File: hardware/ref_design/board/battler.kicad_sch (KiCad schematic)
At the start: 9 parts

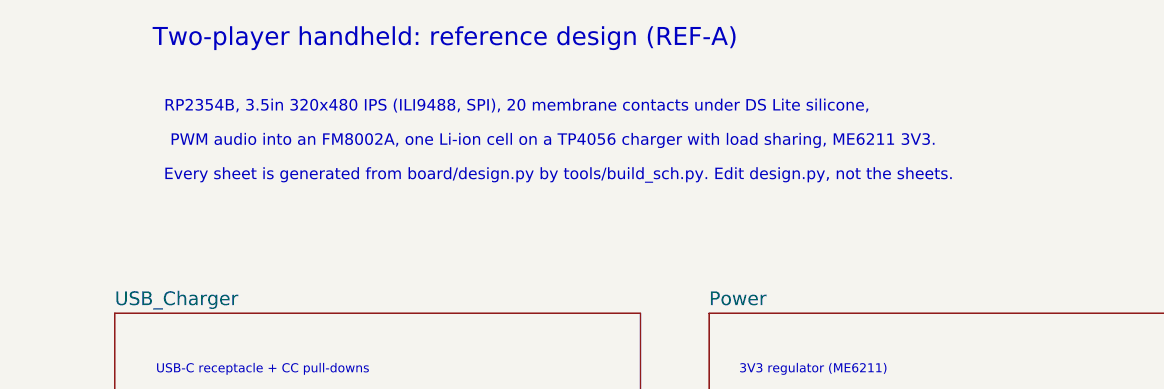
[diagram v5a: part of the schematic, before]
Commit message: ref_design: ER-TFT024IPS-3 panel pin map, R61 2.4k
The 2.4in ST7789V panel on the same 50-pin FPC: K3/K4 on pins 4-5 join
K1/K2's sinks (two LEDs a sink), IM3-0 on pins 6-9 strapped 1110 (4-line
serial II, SDI in and SDO out, as before), D/CX on 36 and SCL on 37.
R61 3.9k -> 2.4k: 0.077 V on 2.2 ohm, 35 mA a sink, 70 mA in all (the
panel's typical, 80 max). Pin review, schematic notes and docs follow.

Co-Authored-By: Claude Opus 5.5 <noreply@anthropic.com>
Claude-Session: https://claude.ai/code/session_01Y3mFMxLYqNeyyedvbYuRwX
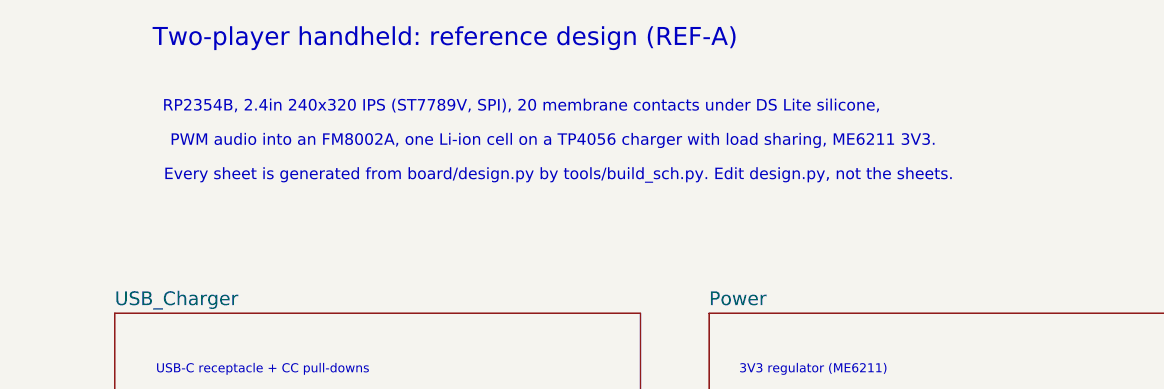
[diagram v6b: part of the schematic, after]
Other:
- note added: "RP2354B, 2.4in 240x320 IPS (ST7789V, SPI), 20 membrane contacts under DS Lite silicone,"
- note removed: "RP2354B, 3.5in 320x480 IPS (ILI9488, SPI), 20 membrane contacts under DS Lite silicone,"
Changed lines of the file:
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@@
 		)
 	)
-	(text "RP2354B, 3.5in 320x480 IPS (ILI9488, SPI), 20 membrane contacts under DS Lite silicone,"
+	(text "RP2354B, 2.4in 240x320 IPS (ST7789V, SPI), 20 membrane contacts under DS Lite silicone,"
 		(exclude_from_sim no)
-		(at 65.0081 27.94 0)
+		(at 65.5218 27.94 0)
 		(effects
 			(font

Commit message: WIP: row 19 layout, one-sided: no speaker, core in the left bezel (unrouted)
Since the one-sided-assembly ruling the work has been row 19, not row 18:
the speaker, J4 and the FM8002A circuit are out of design.py (GPIO8 and
GPIO11 unconnected), the cell sits in its hole, every SMT part is on the
front, and the RP2354B core moved from the back to the left bezel. Row 18
was ruled out on geometry first: with the core on the front it needs most of
one side bezel, and the speaker hole, J4 and three SOIC-8s had nowhere left.

Earlier row-19 placements (core in the right bezel) left 18-30 connections
open after Freerouting: J1's pads faced the cell hole with 1.3 mm to spare,
and seat 2's lines had to cross the whole board past the charger. This
commit has the core and the charger swapped, the hole's lead pocket cut to
1 mm and the original pin map; not routed yet.

Co-Authored-By: Claude Opus 5.5 <noreply@anthropic.com>
Claude-Session: https://claude.ai/code/session_01Y3mFMxLYqNeyyedvbYuRwX
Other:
- removed sheet Audio
- note added: "one Li-ion cell (in a hole in the board) on a TP4056 charger with load sharing, ME6211 3V3, no audio."
- note removed: "PWM audio into an FM8002A, one Li-ion cell on a TP4056 charger with load sharing, ME6211 3V3."
- note removed: "PWM low-pass filter, DC block"
- note removed: "amplifier (FM8002A) and supply"
- note removed: "shutdown control"
- note removed: "speaker pads J4"
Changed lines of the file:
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@@
 		)
 	)
-	(text "PWM audio into an FM8002A, one Li-ion cell on a TP4056 charger with load sharing, ME6211 3V3."
-		(exclude_from_sim no)
-		(at 69.0347 31.75 0)
+	(text "one Li-ion cell (in a hole in the board) on a TP4056 charger with load sharing, ME6211 3V3, no audio."
+		(exclude_from_sim no)
+		(at 71.7283 31.75 0)
 		(effects
 			(font
@@
 		)
 	)
-	(text "PWM low-pass filter, DC block"
-		(exclude_from_sim no)
-		(at 166.632 107.95 0)
-		(effects
-			(font
-				(size 1 1)
-			)
-		)
-	)
-	(text "amplifier (FM8002A) and supply"
-		(exclude_from_sim no)
-		(at 167.0835 112.4 0)
-		(effects
-			(font
-				(size 1 1)
-			)
-		)
-	)
-	(text "shutdown control"
-		(exclude_from_sim no)
-		(at 161.346 116.85 0)
-		(effects
-			(font
-				(size 1 1)
-			)
-		)
-	)
-	(text "speaker pads J4"
-		(exclude_from_sim no)
-		(at 161.108 121.3 0)
-		(effects
-			(font
-				(size 1 1)
-			)
-		)
-	)
 	(text "seat 1 and seat 2 contacts"
 		(exclude_from_sim no)
-		(at 231.433 107.95 0)
+		(at 165.393 107.95 0)
 		(effects
 			(font
@@
 	(text "Start/Select per seat (P1 Start"
 		(exclude_from_sim no)
-		(at 232.9315 112.4 0)
+		(at 166.8915 112.4 0)
 		(effects
 			(font
@@
 	(text "is the power button),"
 		(exclude_from_sim no)
-		(at 228.957 116.85 0)
+		(at 162.917 116.85 0)
 		(effects
 			(font
@@
 	(text "20 contacts, one GPIO each"
 		(exclude_from_sim no)
-		(at 231.647 121.3 0)
+		(at 165.607 121.3 0)
 		(effects
 			(font
@@
 			(color 0 0 0 0)
 		)
-		(property "Sheetname" "Audio"
+		(property "Sheetname" "Buttons"
 			(at 152.4 100.8884 0)
 			(show_name no)
@@
 			)
 		)
-		(property "Sheetfile" "audio.kicad_sch"
+		(property "Sheetfile" "buttons.kicad_sch"
 			(at 152.4 135.2184 0)
 			(show_name no)
@@
 				)
 			)
-		)
-	)
-	(sheet
-		(at 218.44 101.6)
-		(size 58.42 33.02)
-		(exclude_from_sim no)
-		(in_bom yes)
-		(on_board yes)
-		(dnp no)
-		(stroke
-			(width 0.1524)
-			(type solid)
-		)
-		(fill
-			(color 0 0 0 0)
-		)
-		(property "Sheetname" "Buttons"
-			(at 218.44 100.8884 0)
-			(show_name no)
-			(do_not_autoplace no)
-			(effects
-				(font
-					(size 1.524 1.524)
-				)
-				(justify left bottom)
-			)
-		)
-		(property "Sheetfile" "buttons.kicad_sch"
-			(at 218.44 135.2184 0)
-			(show_name no)
-			(do_not_autoplace no)
-			(effects
-				(font
-					(size 1.27 1.27)
-				)
-				(justify left top)
-			)
-		)
-		(instances
-			(project "battler"
-				(path "/8922e0a8-6f76-52f6-b0ec-4de6a784796f"
-					(page "9")
-				)
-			)

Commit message: WIP: speaker on the board's top in the right bezel, audio back; 5 nets unrouted
The FM8002A circuit returns as before row 19 (GPIO8 AUDIO_PWM, GPIO11 AMP_EN,
gain 2, J4 PicoBlade for the speaker's plug). The speaker (15 x 10, hand-fitted)
lies face up in the right bezel below the cell's hole: a rule area keeps parts
(not copper) out of it plus 0.5 mm, outline and label on the silkscreen. J1,
the speaker and J4 with its plug don't all fit in that bezel, so J1 went back up
its wall to the case's own y (beside the hole); usb_pair() drops the pair to the
back beside J1's pads. J4 is machine-placed again (out of NO_ASSEMBLY).

Open: 5 connections (CHG_TEMP, CHG_OFF, CC2_SENSE, SR_CLK, a GND pour island),
route.py --finish crashes in Space() (SwigPyObject), Q3 in the cluster's 0.5 mm
retainer band. case/CELLCUT_FOR_CASE.md has the speaker, grille and J4 notes.

Co-Authored-By: Claude Opus 5.5 <noreply@anthropic.com>
Claude-Session: https://claude.ai/code/session_01Y3mFMxLYqNeyyedvbYuRwX
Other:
- added sheet Audio (audio.kicad_sch)
- note added: "PWM low-pass filter, DC block"
- note added: "amplifier (FM8002A) and supply"
- note added: "one Li-ion cell (in a hole in the board) on a BQ24073 charger, ME6211 3V3, PWM audio into an FM8002A."
- note added: "shutdown control"
- note added: "speaker plug J4"
- note removed: "one Li-ion cell (in a hole in the board) on a TP4056 charger with load sharing, ME6211 3V3, no audio."
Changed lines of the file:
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@@
 		)
 	)
-	(text "one Li-ion cell (in a hole in the board) on a TP4056 charger with load sharing, ME6211 3V3, no audio."
-		(exclude_from_sim no)
-		(at 71.7283 31.75 0)
+	(text "one Li-ion cell (in a hole in the board) on a BQ24073 charger, ME6211 3V3, PWM audio into an FM8002A."
+		(exclude_from_sim no)
+		(at 73.1774 31.75 0)
 		(effects
 			(font
@@
 		)
 	)
+	(text "PWM low-pass filter, DC block"
+		(exclude_from_sim no)
+		(at 166.632 107.95 0)
+		(effects
+			(font
+				(size 1 1)
+			)
+		)
+	)
+	(text "amplifier (FM8002A) and supply"
+		(exclude_from_sim no)
+		(at 167.0835 112.4 0)
+		(effects
+			(font
+				(size 1 1)
+			)
+		)
+	)
+	(text "shutdown control"
+		(exclude_from_sim no)
+		(at 161.346 116.85 0)
+		(effects
+			(font
+				(size 1 1)
+			)
+		)
+	)
+	(text "speaker plug J4"
+		(exclude_from_sim no)
+		(at 160.965 121.3 0)
+		(effects
+			(font
+				(size 1 1)
+			)
+		)
+	)
 	(text "seat 1 and seat 2 contacts"
 		(exclude_from_sim no)
-		(at 165.393 107.95 0)
+		(at 231.433 107.95 0)
 		(effects
 			(font
@@
 	(text "Start/Select per seat (P1 Start"
 		(exclude_from_sim no)
-		(at 166.8915 112.4 0)
+		(at 232.9315 112.4 0)
 		(effects
 			(font
@@
 	(text "is the power button),"
 		(exclude_from_sim no)
-		(at 162.917 116.85 0)
+		(at 228.957 116.85 0)
 		(effects
 			(font
@@
 	(text "20 contacts, one GPIO each"
 		(exclude_from_sim no)
-		(at 165.607 121.3 0)
+		(at 231.647 121.3 0)
 		(effects
 			(font
@@
 			(color 0 0 0 0)
 		)
+		(property "Sheetname" "Audio"
+			(at 152.4 100.8884 0)
+			(show_name no)
+			(do_not_autoplace no)
+			(effects
+				(font
+					(size 1.524 1.524)
+				)
+				(justify left bottom)
+			)
+		)
+		(property "Sheetfile" "audio.kicad_sch"
+			(at 152.4 135.2184 0)
+			(show_name no)
+			(do_not_autoplace no)
+			(effects
+				(font
+					(size 1.27 1.27)
+				)
+				(justify left top)
+			)
+		)
+		(instances
+			(project "battler"
+				(path "/8922e0a8-6f76-52f6-b0ec-4de6a784796f"
+					(page "8")
+				)
+			)
+		)
+	)
+	(sheet
+		(at 218.44 101.6)
+		(size 58.42 33.02)
+		(exclude_from_sim no)
+		(in_bom yes)
+		(on_board yes)
+		(dnp no)
+		(stroke
+			(width 0.1524)
+			(type solid)
+		)
+		(fill
+			(color 0 0 0 0)
+		)
 		(property "Sheetname" "Buttons"
-			(at 152.4 100.8884 0)
+			(at 218.44 100.8884 0)
 			(show_name no)
 			(do_not_autoplace no)
@@
 		)
 		(property "Sheetfile" "buttons.kicad_sch"
-			(at 152.4 135.2184 0)
+			(at 218.44 135.2184 0)
 			(show_name no)
 			(do_not_autoplace no)
@@
 			(project "battler"
 				(path "/8922e0a8-6f76-52f6-b0ec-4de6a784796f"
-					(page "8")
-				)
-			)
+					(page "9")
+				)
+			)
